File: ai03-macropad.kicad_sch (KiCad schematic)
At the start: 0 parts

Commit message: finished sch and fp assigned. pcb ready
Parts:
- added C1: 1uF, Capacitor_SMD:C_0805_2012Metric, symbol Device:C_Small
- added C2, C3, C4: 0.1uF, Capacitor_SMD:C_0805_2012Metric, symbol Device:C_Small
- added C5: 10uF, Capacitor_SMD:C_0805_2012Metric, symbol Device:C_Small
- added C6, C7: 22pF, Capacitor_SMD:C_0805_2012Metric, symbol Device:C_Small
- added D1, D2, D3, D4: 1N4148W, Diode_SMD:D_SOD-123, symbol Diode:1N4148W
- added F1: 500mA, Fuse:Fuse_1206_3216Metric, symbol Device:Polyfuse_Small
- added MX1, MX2, MX3, MX4: MX-NoLED, MX_Alps_Hybrid:MX-1U-NoLED, symbol MX_Alps_Hybrid:MX-NoLED
- added R1, R4: 10k, Resistor_SMD:R_0805_2012Metric, symbol Device:R_Small
- added R2, R3: 22, Resistor_SMD:R_0805_2012Metric, symbol Device:R_Small
- added SW1: SW_Push, random-keyboard-parts:SKQG-1155865, symbol Switch:SW_Push
- added U1: ATmega32U4-A, Package_QFP:TQFP-44_10x10mm_P0.8mm, symbol MCU_Microchip_ATmega:ATmega32U4-A
- added USB1: Molex-0548190589, random-keyboard-parts:Molex-0548190589, symbol random-keyboard-parts:Molex-0548190589
- added Y1: 16MHz, Crystal:Crystal_SMD_3225-4Pin_3.2x2.5mm, symbol Device:Crystal_GND24_Small
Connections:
- new net: D1.2 (A), MX1.2 (ROW)
- new net: D4.2 (A), MX4.2 (ROW)
- new net: C7.2, U1.16 (XTAL2), Y1.3
- new net: R3.2, U1.3 (D-)
- new net: R2.2, U1.4 (D+)
- new net: C1.1, U1.6 (UCAP)
- new net: D2.2 (A), MX2.2 (ROW)
- new net: C6.2, U1.17 (XTAL1), Y1.1
- new net: D3.2 (A), MX3.2 (ROW)
- new net: R4.2, SW1.2, U1.13 (~{RESET})
- new net: R1.1, U1.33 (~{HWB}/PE2)
- new net +5V: C2.1, C3.1, C4.1, C5.1, F1.2, R4.1, U1.14 (VCC), U1.2 (UVCC), U1.24 (AVCC), U1.34 (VCC), U1.44 (AVCC), U1.7 (VBUS)
- new net D+: R2.1, USB1.3 (D+)
- new net D-: R3.1, USB1.4 (D-)
- new net GND: C1.2, C2.2, C3.2, C4.2, C5.2, C6.1, C7.1, R1.2, SW1.1, U1.15 (GND), U1.23 (GND), U1.35 (GND), U1.43 (GND), U1.5 (UGND), USB1.1 (GND), Y1.2, Y1.4
- new net VCC: F1.1, USB1.5 (VBUS)
- new net col0: MX1.1 (COL), MX3.1 (COL)
- new net col1: MX2.1 (COL), MX4.1 (COL)
- new net row0: D1.1 (K), D2.1 (K)
- new net row1: D3.1 (K), D4.1 (K)
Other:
- note added: "Decoupling Capaciors (filter out noise from mvc)"
- note added: "Operating Volage"
- note added: "usb circuitry"

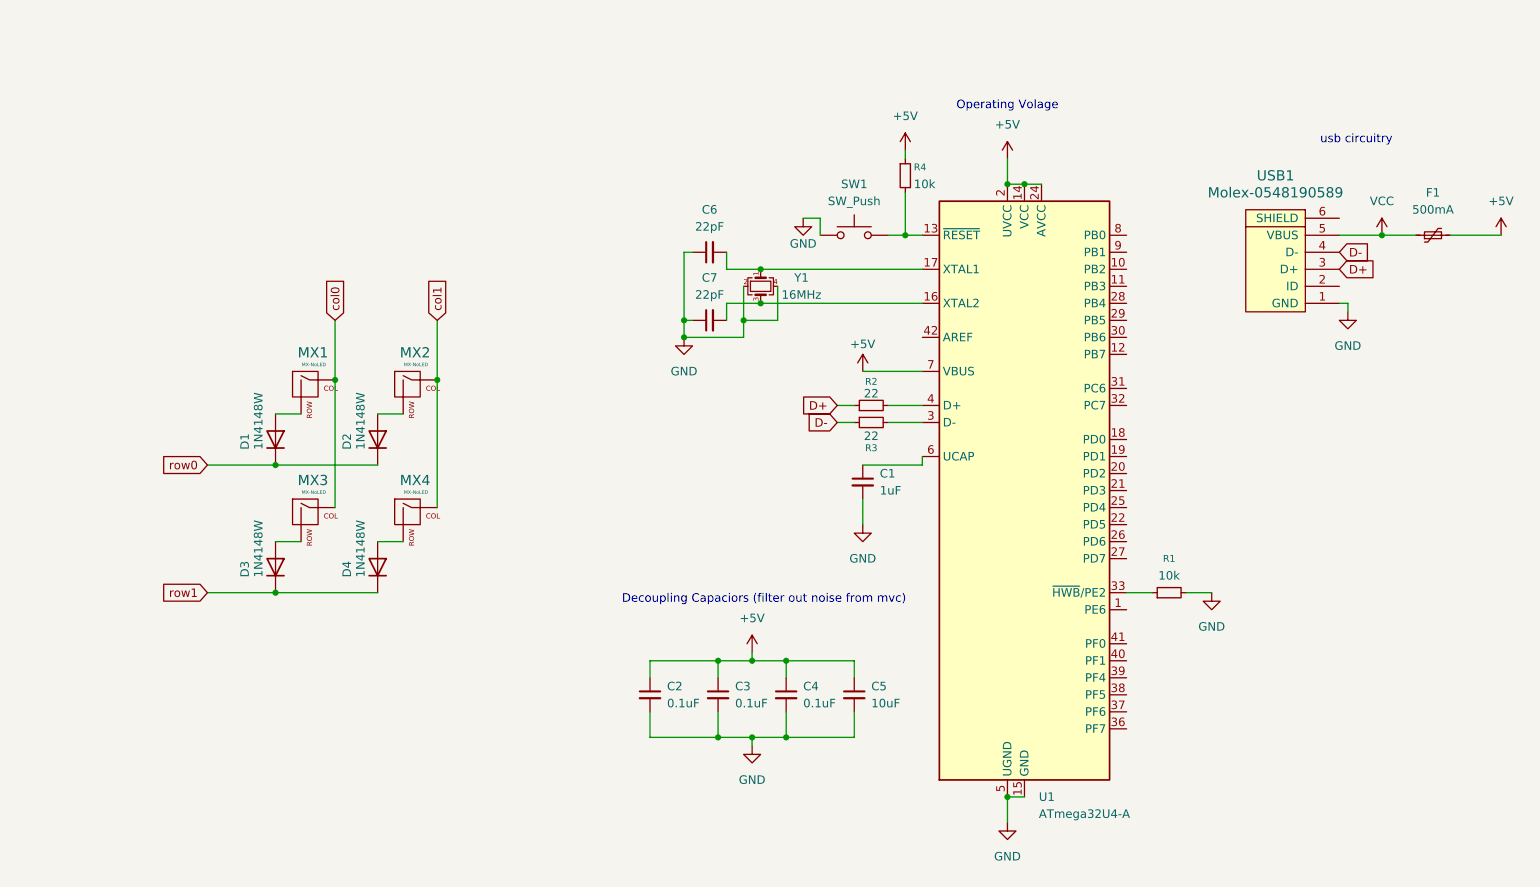
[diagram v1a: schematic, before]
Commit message: small changes to sch, switch placement for pcb
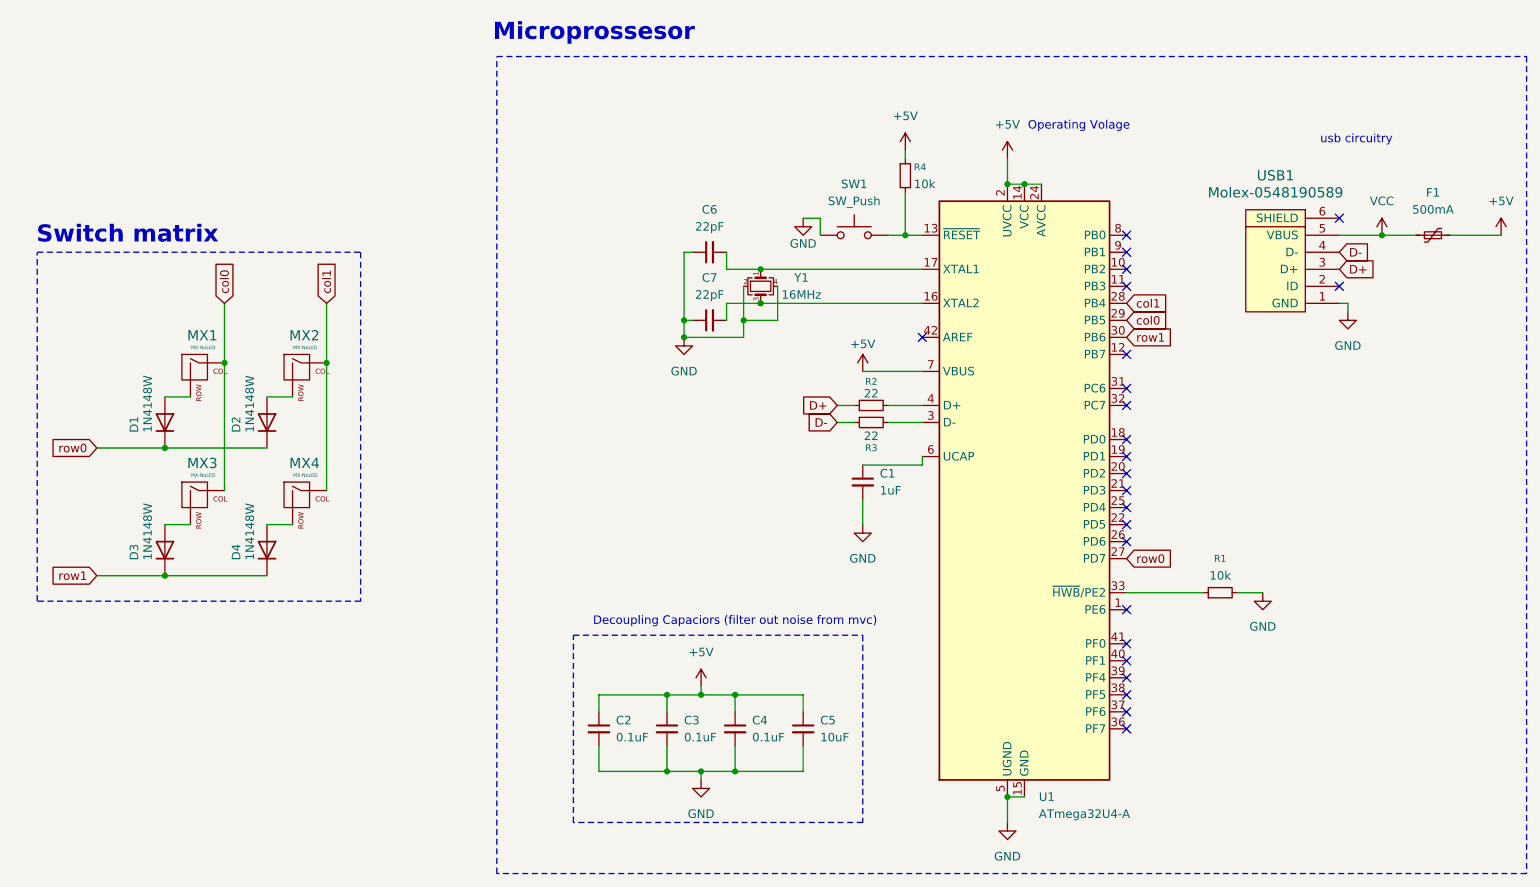
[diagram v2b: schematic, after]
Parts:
- MX1, MX2, MX3, MX4: footprint MX_Alps_Hybrid:MX-1U-NoLED -> MX_Alps_Hybrid:MX-1U
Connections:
- net col0: now also U1.29 (PB5)
- net col1: now also U1.28 (PB4)
- net row0: now also U1.27 (PD7)
- net row1: now also U1.30 (PB6)
- no-connect marks 0 -> 24
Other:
- note added: "Microprossesor"
- note added: "Switch matrix"
- title: (none) -> ai03 Keyboard PCB
- moved on the sheet: C2, C3, C4, C5, D1, D2, D3, D4, MX1, MX2, MX3, MX4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
